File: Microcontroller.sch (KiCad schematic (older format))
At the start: 6 parts, among them J13 640456-3, J14 640456-3, J15 640456-3, J16 B5B-XH-A_LF__SN_, J17 0022232041, U11 STM32H743ZIT6

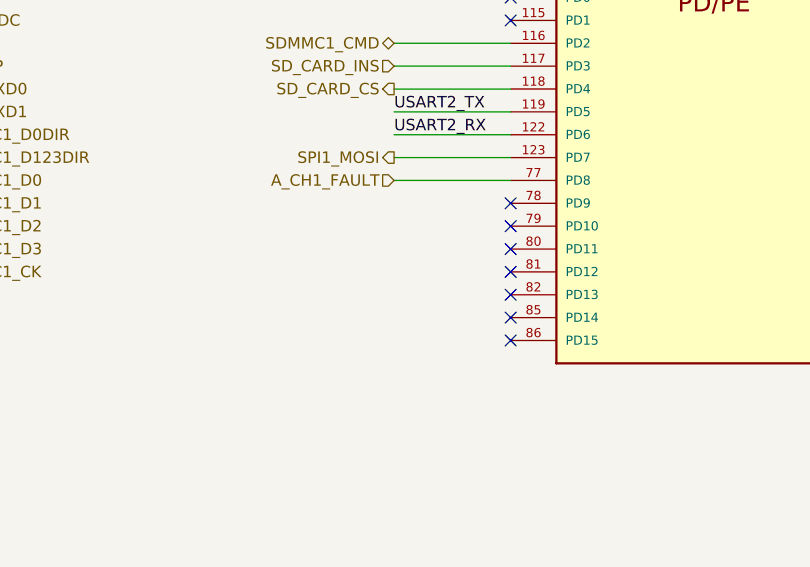
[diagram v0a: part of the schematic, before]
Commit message: RTC DS3231 layot finished
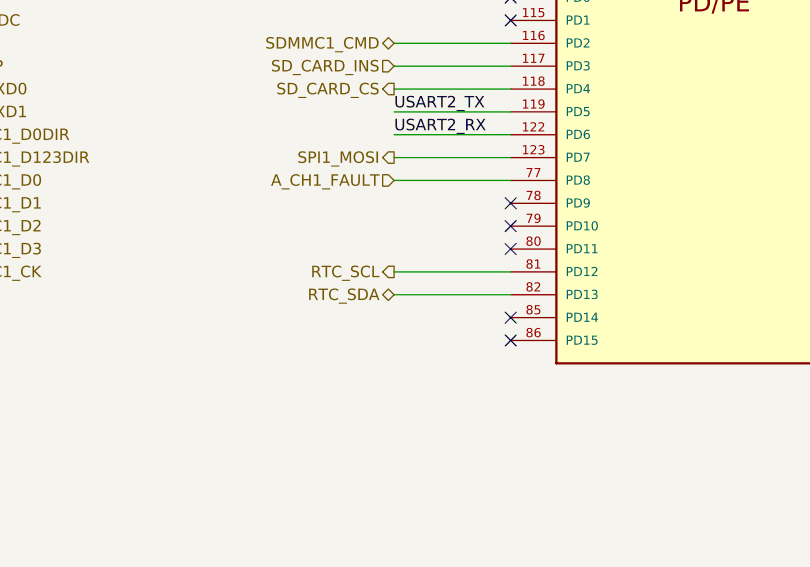
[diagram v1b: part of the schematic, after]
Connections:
- net RTC_SCL: now reaches U11.81 (PD12)
- net RTC_SDA: now reaches U11.82 (PD13)
- no-connect marks 46 -> 44
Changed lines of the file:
@@
 	8950 1310 8440 1310
 NoConn ~ 6640 2410
-NoConn ~ 6640 2510
-NoConn ~ 6640 2610
 Text HLabel 8950 1410 2    50   Output ~ 0
 SKIP_N_UNLOADED_BEEPER
@@
 	6130 5340 6640 5340
 NoConn ~ 6640 5440
+Text HLabel 6130 2510 0    50   Output ~ 0
+RTC_SCL
+Text HLabel 6130 2610 0    50   BiDi ~ 0
+RTC_SDA
+Wire Wire Line
+	6130 2510 6640 2510
+Wire Wire Line
+	6130 2610 6640 2610
 $EndSCHEMATC

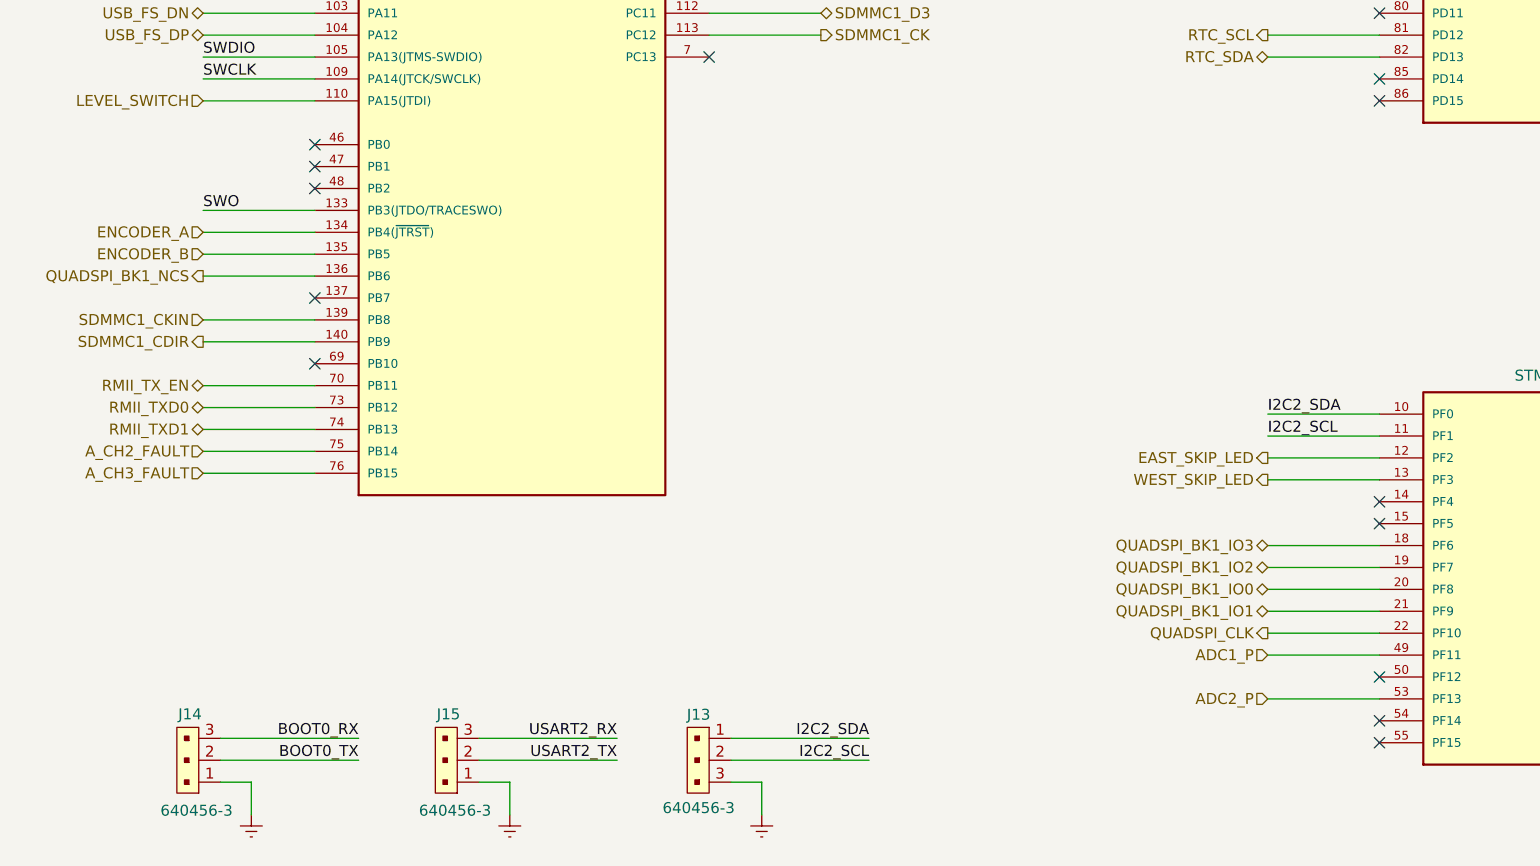
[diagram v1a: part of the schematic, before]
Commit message: ADC2 in changed to IN5
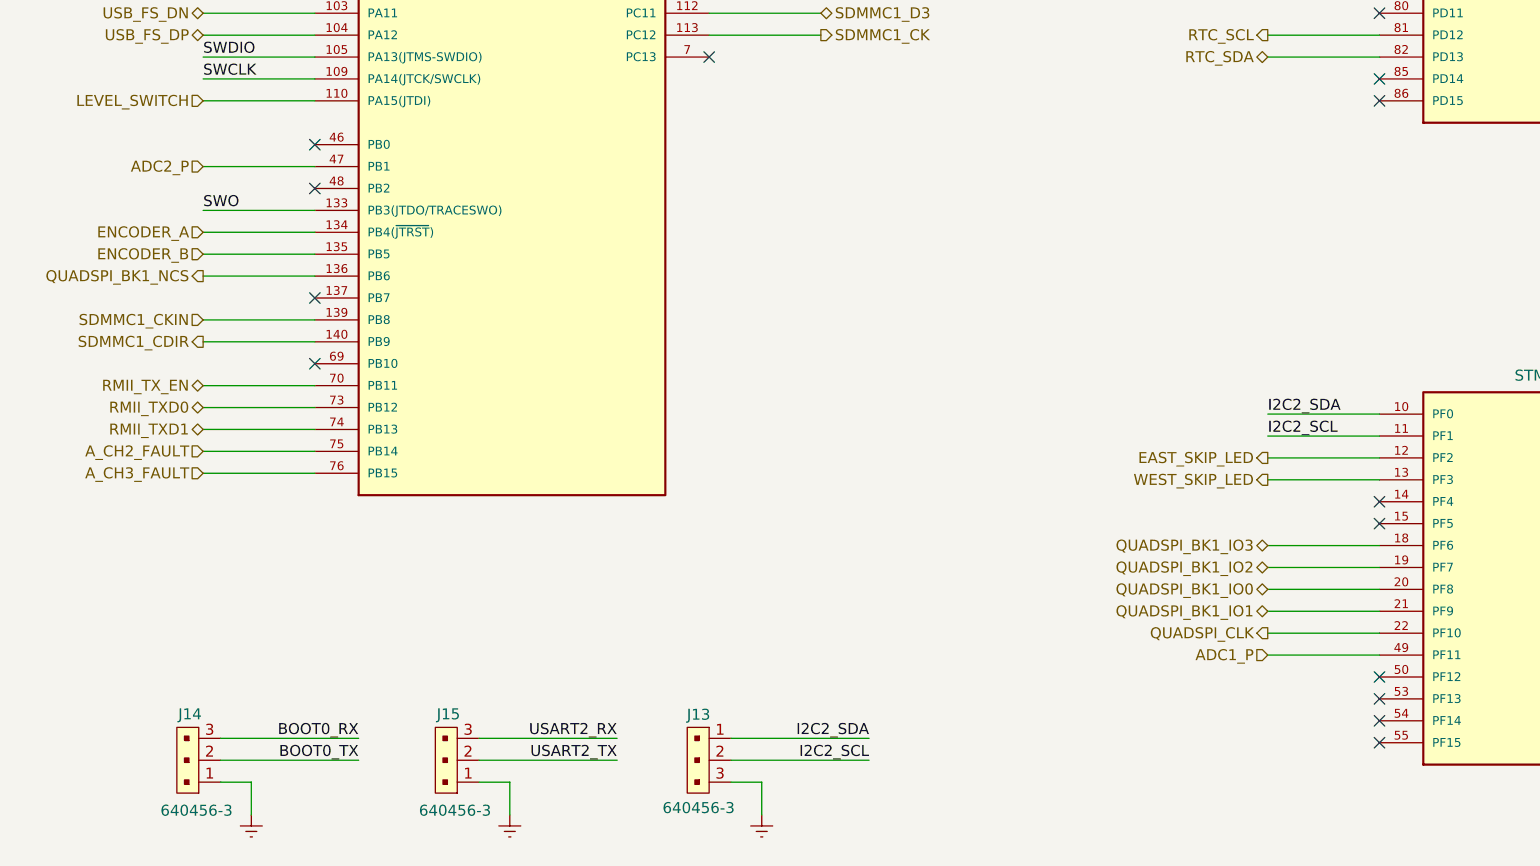
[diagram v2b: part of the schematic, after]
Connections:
- net ADC2_P: now also U11.47 (PB1); no longer U11.53 (PF13)
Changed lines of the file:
@@
 SWCLK
 NoConn ~ 1780 3010
-NoConn ~ 1780 3110
 NoConn ~ 1780 3210
 Wire Wire Line
@@
 Text HLabel 6130 5340 0    50   Input ~ 0
 ADC1_P
-Text HLabel 6130 5540 0    50   Input ~ 0
+Text HLabel 1270 3110 0    50   Input ~ 0
 ADC2_P
 Wire Wire Line
-	6130 5540 6640 5540
+	1270 3110 1780 3110
 Text HLabel 1270 4410 0    50   Input ~ 0
 A_CH2_FAULT
@@
 Wire Wire Line
 	6130 2610 6640 2610
+NoConn ~ 6640 5540
 $EndSCHEMATC
